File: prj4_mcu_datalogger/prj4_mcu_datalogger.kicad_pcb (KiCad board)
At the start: 2 copper layers, 29 parts, among them J1 Conn_01x04_Pin, J2 Conn_01x04_Pin, J3 Conn_01x09_Pin, J4 Conn_02x03_Odd_Even, U1 DS1337S+, U2 ATMEGA328P-AU, U3 24LC1025, U4 24LC1025, Y1 32.768 KHz, Y2 16 MHz

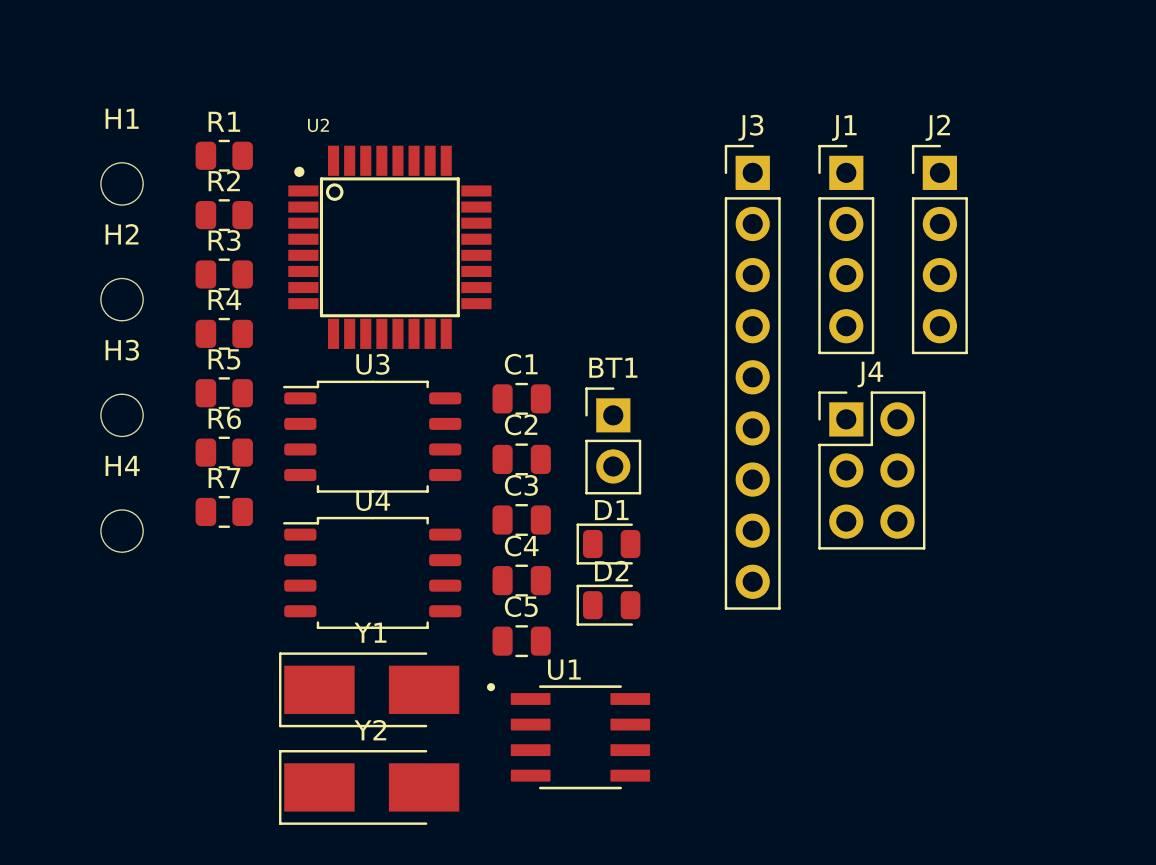
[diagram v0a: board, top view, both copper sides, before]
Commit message: Introdotti i componenti nello schema
Feat: inseriti i componenti nel PCB e posizionati
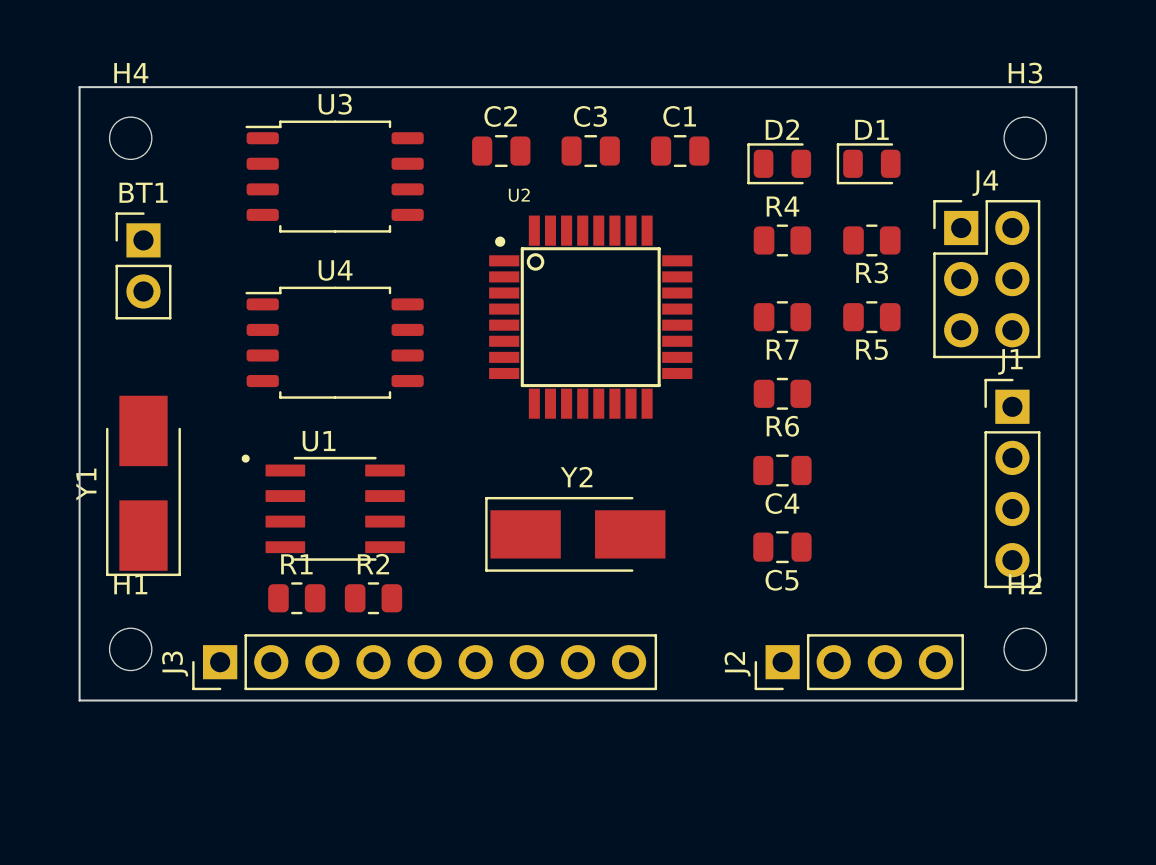
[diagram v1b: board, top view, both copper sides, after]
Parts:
- moved H2 48.1 mm to (174.0, 108.0)
- moved H3 46.9 mm to (174.0, 82.5)
- moved J3 35.9 mm to (134.0, 108.6), turned to 90 degrees
- moved R5 32.4 mm to (166.4, 91.4), turned to 180 degrees
- moved R3 32.2 mm to (166.4, 87.6), turned to 180 degrees
- moved R7 29.4 mm to (161.9, 91.4), turned to 180 degrees
- moved R4 28.1 mm to (161.9, 87.6)
- moved R6 27.9 mm to (161.9, 95.2), turned to 180 degrees
- moved J2 25.5 mm to (161.9, 108.6), turned to 90 degrees
- moved BT1 24.9 mm to (130.2, 87.6)
- moved D2 23.5 mm to (161.9, 83.8)
- moved H1 23.1 mm to (129.5, 108.0)
- moved D1 22.9 mm to (166.4, 83.8)
- moved R1 22.3 mm to (137.8, 105.4)
- moved R2 20.4 mm to (141.6, 105.4)
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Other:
- board outline added: 49.5 x 30.5 mm

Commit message: Sistemate le dimensioni del PCB
Feat: ridotte al minimo le dimensioni del PCB
Feat: spostati i mounting hole
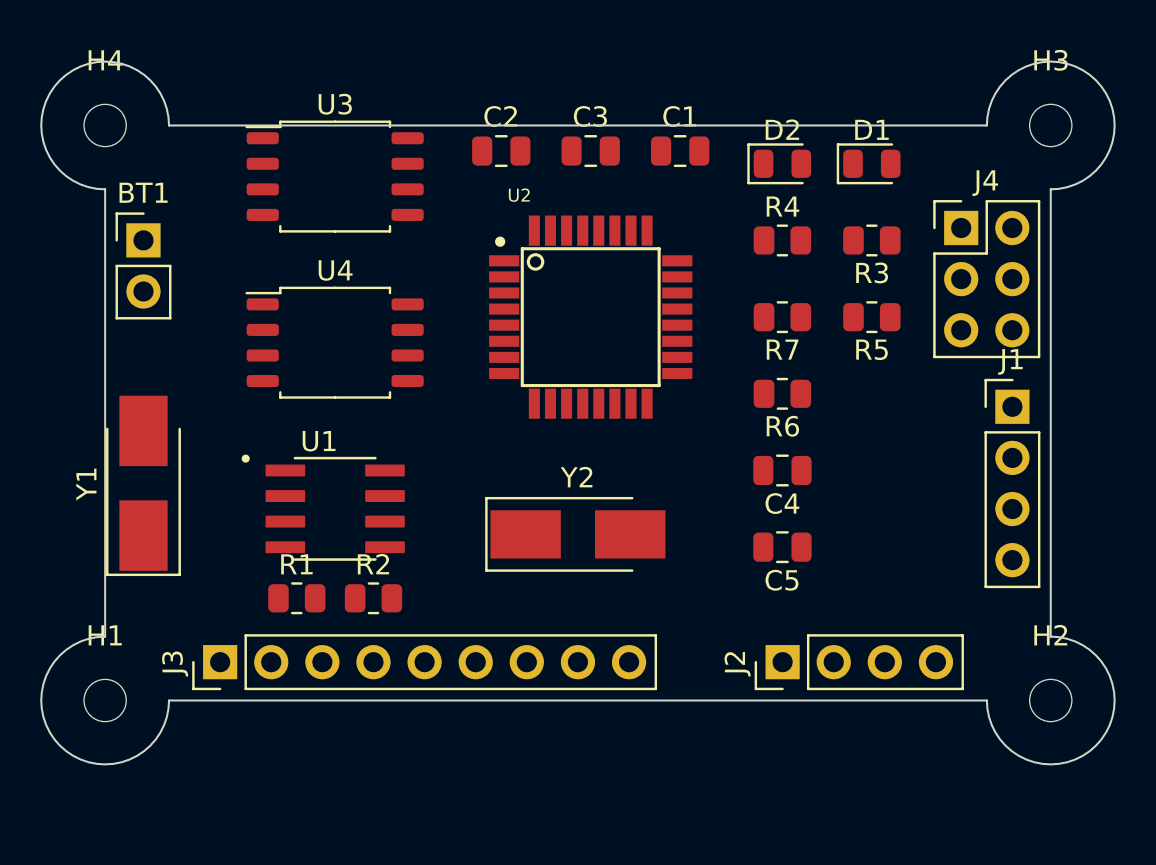
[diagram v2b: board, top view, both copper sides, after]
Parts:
- moved H1 2.84 mm to (128.3, 110.5)
- moved H2 2.84 mm to (175.3, 110.5)
- moved H3 1.42 mm to (175.3, 81.9)
- moved H4 1.42 mm to (128.3, 81.9)
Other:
- board size 49.5 x 30.5 mm -> 53.3 x 34.9 mm
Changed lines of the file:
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@@
   )
   (footprint "MountingHole:MountingHole_2.1mm" (layer "F.Cu")
-    (at 129.54 82.55)
+    (at 128.27 81.915)
     (descr "Mounting Hole 2.1mm, no annular")
     (tags "mounting hole 2.1mm no annular")
@@
   )
   (footprint "MountingHole:MountingHole_2.1mm" (layer "F.Cu")
-    (at 173.99 82.55)
+    (at 175.26 81.915)
     (descr "Mounting Hole 2.1mm, no annular")
     (tags "mounting hole 2.1mm no annular")
@@
   )
   (footprint "MountingHole:MountingHole_2.1mm" (layer "F.Cu")
-    (at 173.99 107.95)
+    (at 175.26 110.49)
     (descr "Mounting Hole 2.1mm, no annular")
     (tags "mounting hole 2.1mm no annular")
@@
   )
   (footprint "MountingHole:MountingHole_2.1mm" (layer "F.Cu")
-    (at 129.54 107.95)
+    (at 128.27 110.49)
     (descr "Mounting Hole 2.1mm, no annular")
     (tags "mounting hole 2.1mm no annular")
@@
     )
   )
-  (gr_rect (start 127 80.01) (end 176.53 110.49)
-    (stroke (width 0.1) (type default)) (fill none) (layer "Edge.Cuts"))
+  (gr_line (start 175.26 107.315) (end 175.26 85.09)
+    (stroke (width 0.1) (type default)) (layer "Edge.Cuts"))
+  (gr_line (start 128.27 85.09) (end 128.27 107.315)
+    (stroke (width 0.1) (type default)) (layer "Edge.Cuts"))
+  (gr_arc (start 128.27 85.09) (mid 126.024936 79.669936) (end 131.445 81.915)
+    (stroke (width 0.1) (type default)) (layer "Edge.Cuts"))
+  (gr_arc (start 131.445 110.49) (mid 126.024936 112.735064) (end 128.27 107.315)
+    (stroke (width 0.1) (type default)) (layer "Edge.Cuts"))
+  (gr_arc (start 172.085 81.915) (mid 177.505064 79.669936) (end 175.26 85.09)
+    (stroke (width 0.1) (type default)) (layer "Edge.Cuts"))
+  (gr_line (start 131.445 110.49) (end 172.085 110.49)
+    (stroke (width 0.1) (type default)) (layer "Edge.Cuts"))
+  (gr_line (start 172.085 81.915) (end 131.445 81.915)
+    (stroke (width 0.1) (type default)) (layer "Edge.Cuts"))
+  (gr_arc (start 175.26 107.315) (mid 177.505064 112.735064) (end 172.085 110.49)
+    (stroke (width 0.1) (type default)) (layer "Edge.Cuts"))
 )

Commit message: Completate le connessioni tra i componenti del PCB
Feat: connessi i vari componenti del PCB
Feat: effettuato DRC per verifica correttezza
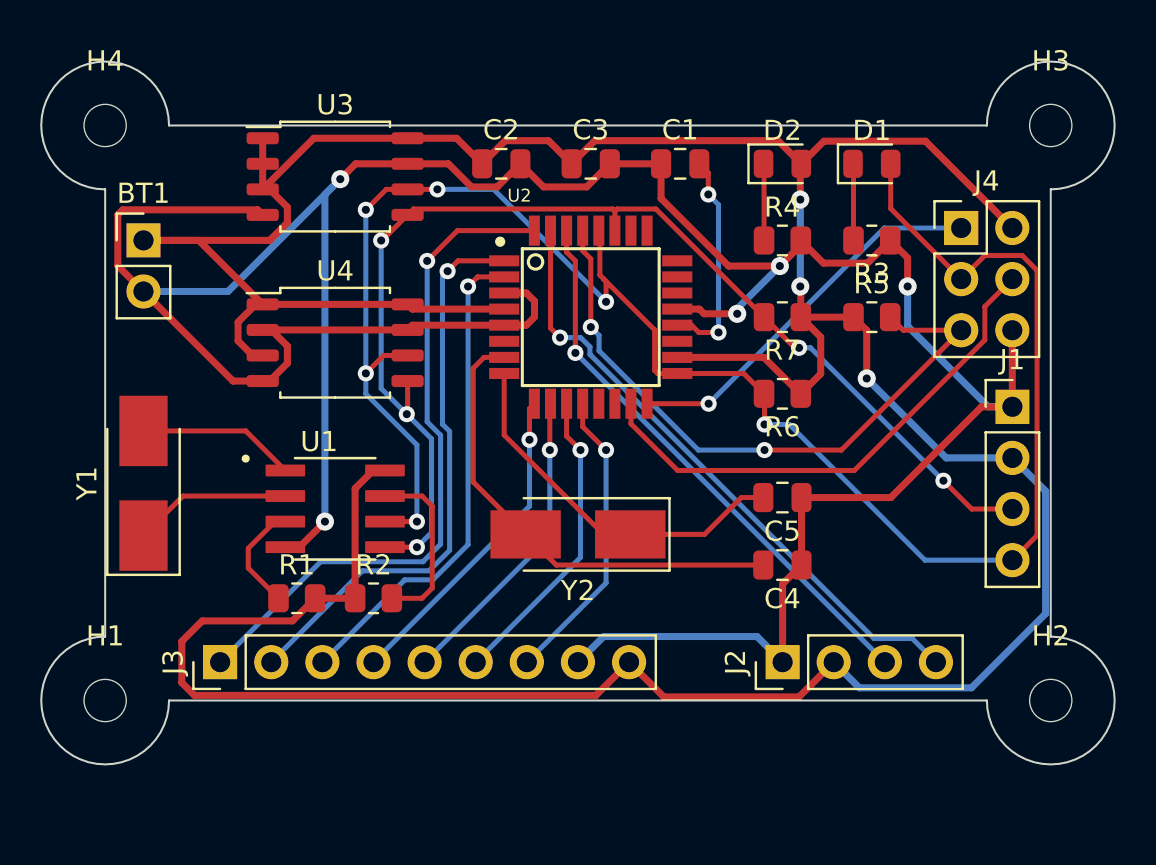
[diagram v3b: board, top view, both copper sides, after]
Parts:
- moved C4 4.70 mm to (161.9, 103.8)
- moved C5 2.46 mm to (161.9, 100.4)
- moved C1 0.63 mm to (156.8, 83.8)
- moved C2 0.63 mm to (148.0, 83.8)
- moved C3 0.63 mm to (152.4, 83.8)
- turned R5 to 0 degrees
- turned Y2 to 180 degrees
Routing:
- net /Vcc: track 0.00 -> 187.4 mm, vias 0 -> 3
- net GND: track 0.00 -> 159.7 mm, vias 0 -> 5
- net /SCK: track 0.00 -> 93.8 mm, vias 0 -> 6
- net /SDA: track 0.00 -> 59.1 mm, vias 0 -> 5
- net /D2: track 0.00 -> 33.7 mm, vias 0 -> 1
- net /RESET: track 0.00 -> 32.6 mm, vias 0 -> 2
- net /TX: track 0.00 -> 31.1 mm, vias 0 -> 1
- net /D3: track 0.00 -> 28.3 mm, vias 0 -> 1
- net /RX: track 0.00 -> 28.0 mm, vias 0 -> 1
- net /MOSI: track 0.00 -> 25.8 mm
- net /D4: track 0.00 -> 24.5 mm, vias 0 -> 1
- net Net-(U2-PB6): track 0.00 -> 23.5 mm
- net /MISO: track 0.00 -> 19.2 mm, vias 0 -> 1
- net Net-(U2-PB7): track 0.00 -> 18.7 mm
- net /D5: track 0.00 -> 16.2 mm, vias 0 -> 1
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
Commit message: Inseriti copper fill
Feat: aggiunto copper fill per GND e Vcc
Fix: rimosso warning relativo alla silkscreen di U3
Fix: rimosso warning relativo a una pista di lunghezza 0
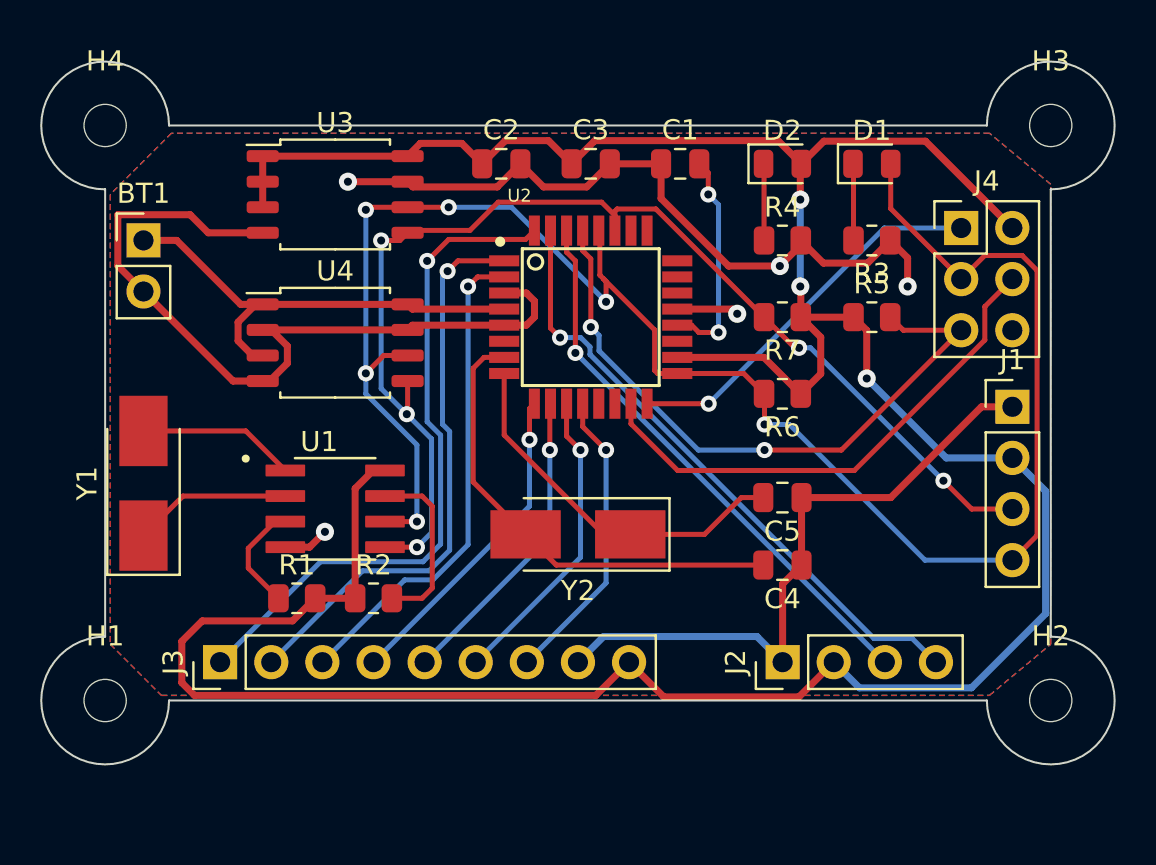
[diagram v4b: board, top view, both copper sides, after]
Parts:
- moved U3 0.89 mm to (139.7, 85.3)
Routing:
- net GND: track 159.7 -> 113.5 mm
- net /Vcc: track 187.4 -> 176.6 mm
- net /SDA: track 59.1 -> 60.2 mm
- net /SCK: track 93.8 -> 93.0 mm
- added copper zone on F.Cu, net /Vcc
- added copper zone on B.Cu, net GND

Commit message: Completata silkscreen
Feat: aggiunti testi
Feat: aggiunti loghi
Fix: sistemate le sovrapposizioni
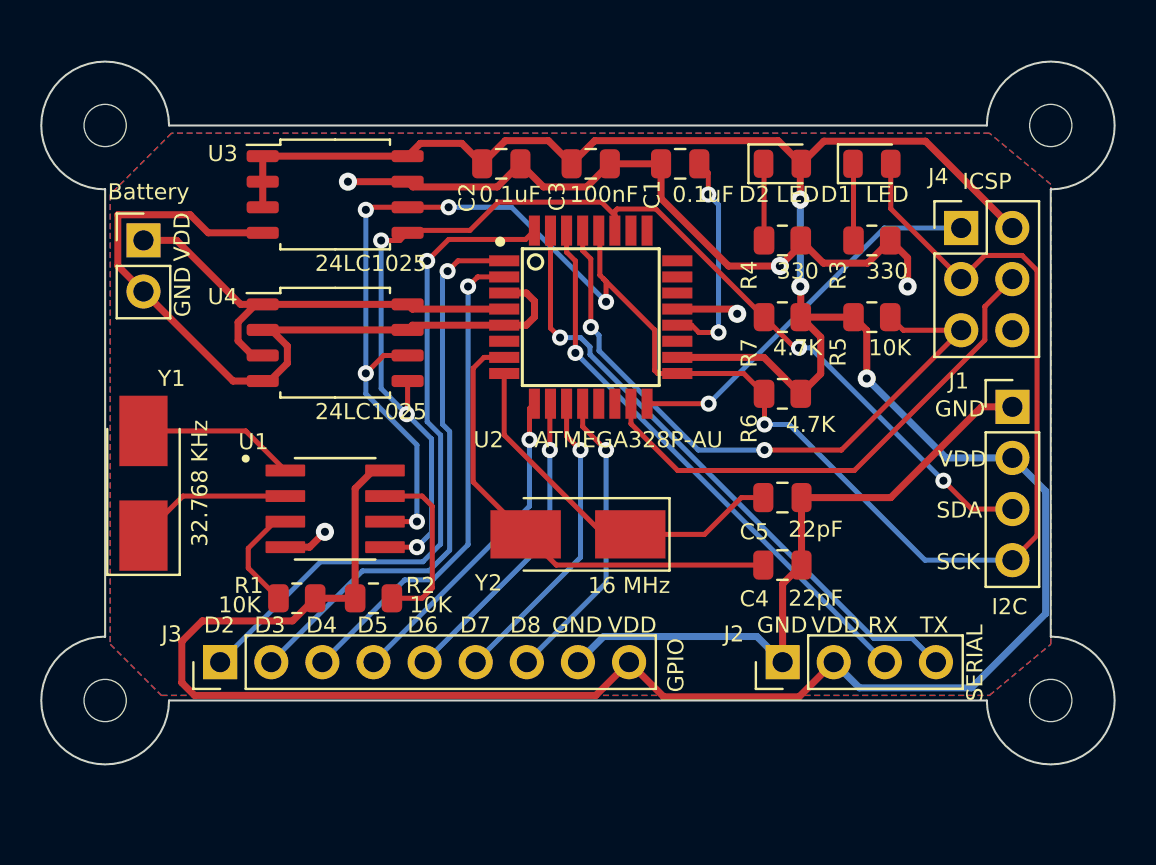
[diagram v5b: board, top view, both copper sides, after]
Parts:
- added REF**: OSHW-Logo2_7.3x6mm_SilkScreen, Symbol:OSHW-Logo2_7.3x6mm_SilkScreen, B.Cu at (136.1, 91.6)
- added REF**: KiCad-Logo2_5mm_SilkScreen, Symbol:KiCad-Logo2_5mm_SilkScreen, B.Cu at (139.3, 85.5)
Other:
- board text added: "- 2Mbit EEPROM - RTC - I2C, SPI, GPIOs"
- board text added: "D2"
- board text added: "D3"
- board text added: "D4"
- board text added: "D5"
- board text added: "D6"
- board text added: "D7"
- board text added: "D8"
- board text added: "Data Logger with the ATMega328P"
- board text added: "GND"
- board text added: "GPIO"
- board text added: "I2C"
- board text added: "ICSP"
- board text added: "RX"
- board text added: "SCK"
- board text added: "SDA"
- board text added: "SERIAL"
- board text added: "TX"
- board text added: "VDD"

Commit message: Correzione SCK
Fix: SCL era nominato SCK (erano in corto), ora sono separati
Fix: numerati i REF degli elementi grafici su Pcbnew
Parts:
- renumbered REF** to REF1, REF** to REF2
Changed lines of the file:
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@@
     (tags "Logo Symbol OSHW")
     (attr exclude_from_pos_files exclude_from_bom)
-    (fp_text reference "REF**" (at 0 0) (layer "B.SilkS") hide
+    (fp_text reference "REF2" (at 0 0) (layer "B.SilkS") hide
         (effects (font (size 1 1) (thickness 0.15)) (justify mirror))
     )
@@
     (tags "Logo KiCad")
     (attr exclude_from_pos_files exclude_from_bom)
-    (fp_text reference "REF**" (at 0 5.08) (layer "B.SilkS") hide
+    (fp_text reference "REF1" (at 0 5.08) (layer "B.SilkS") hide
         (effects (font (size 1 1) (thickness 0.15)) (justify mirror))
     )

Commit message: Correzione connessioni sul PCB
Fix: rifatti i collegamenti di SCL e SCK
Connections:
- J1 pad 4: /SCK -> /SCL
- R6 pad 2: /SCK -> /SCL
- U1 pad 6: /SCK -> /SCL
- U2 pad 28: /SCK -> /SCL
- U3 pad 6: /SCK -> /SCL
- U4 pad 6: /SCK -> /SCL
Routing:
- net /SCK: track 93.0 -> 24.7 mm, vias 6 -> 1
- net /SCL: track 0.00 -> 67.4 mm, vias 0 -> 6

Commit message: Aggiunte informazioni - progetto completato
Feat: aggiunte informazioni sul PCB
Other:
- board text added: "0,2000 mm / 0,0000 mm"
- board text added: "0,3000 mm"
- board text added: "1,6000 mm"
- board text added: "2"
- board text added: "53,3400 mm x 34,9250 mm"
- board text added: "BOARD CHARACTERISTICS"
- board text added: "Board Thickness:"
- board text added: "Board overall dimensions:"
- board text added: "Castellated pads:"
- board text added: "Copper Finish:"
- board text added: "Copper Layer Count:"
- board text added: "Edge card connectors:"
- board text added: "Impedance Control:"
- board text added: "Min hole diameter:"
- board text added: "Min track/spacing:"
- board text added: "No"
- board text added: "None"
- board text added: "Plated Board Edge:"
